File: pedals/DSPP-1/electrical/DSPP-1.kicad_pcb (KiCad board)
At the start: 2 copper layers, 4 parts, among them U1 STM32H747IGTx, U3 PCM3060, U4 STM32G4A1CETx, U5 STM32F401CBUx

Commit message: schematic update for MCU, Codec
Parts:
- removed U5: STM32F401CBUx, Package_DFN_QFN:QFN-48-1EP_7x7mm_P0.5mm_EP5.6x5.6mm
- added C10: 100n, Capacitor_SMD:C_0805_2012Metric, F.Cu at (148.9, 105.3)
- added C11: 10u, Capacitor_SMD:C_0805_2012Metric, F.Cu at (148.9, 108.3)
- added C12: 10u, Capacitor_SMD:C_0805_2012Metric, F.Cu at (148.9, 111.3)
- added C13: 100n, Capacitor_SMD:C_0805_2012Metric, F.Cu at (148.9, 114.3)
- added C14: 100n, Capacitor_SMD:C_0805_2012Metric, F.Cu at (153.3, 102.3)
- added C15: 10u, Capacitor_SMD:C_0805_2012Metric, F.Cu at (153.3, 105.3)
- added C16: 10u, Capacitor_SMD:C_0805_2012Metric, F.Cu at (153.3, 108.3)
- added C2: 100n, Capacitor_SMD:C_0805_2012Metric, F.Cu at (144.4, 102.3)
- added C3: 10u, Capacitor_SMD:C_0805_2012Metric, F.Cu at (144.4, 105.3)
- added C4: 10u, Capacitor_SMD:C_0805_2012Metric, F.Cu at (144.4, 108.3)
- added C5: 100p, Capacitor_SMD:C_0805_2012Metric, F.Cu at (144.4, 111.3)
- added C6: 100n, Capacitor_SMD:C_0805_2012Metric, F.Cu at (144.4, 114.3)
- added C7: 2.2n, Capacitor_SMD:C_0805_2012Metric, F.Cu at (148.9, 102.3)
- added J1: Guitar Jack, Connector_Audio:Jack_6.35mm_Neutrik_NMJ6HCD2_Horizontal, F.Cu at (150.1, 82.0)
- added JP1: Jumper, Jumper:SolderJumper-3_P1.3mm_Open_RoundedPad1.0x1.5mm, F.Cu at (158.4, 102.6)
- added JP2: Jumper, Jumper:SolderJumper-3_P1.3mm_Open_RoundedPad1.0x1.5mm, F.Cu at (158.4, 106.4)
- added JP3: Jumper, Jumper:SolderJumper-3_P1.3mm_Open_RoundedPad1.0x1.5mm, F.Cu at (158.4, 110.2)
- added R10: 100R, Resistor_SMD:R_0805_2012Metric, F.Cu at (177.4, 83.9)
- added R11: 0/220k, Resistor_SMD:R_0805_2012Metric, F.Cu at (177.4, 86.9)
- added R12: 10k, Resistor_SMD:R_0805_2012Metric, F.Cu at (177.4, 89.8)
- added R13: 10k, Resistor_SMD:R_0805_2012Metric, F.Cu at (177.4, 92.8)
- added R3: 100k, Resistor_SMD:R_0805_2012Metric, F.Cu at (173.0, 81.0)
- added R4: 100k, Resistor_SMD:R_0805_2012Metric, F.Cu at (173.0, 83.9)
- added R5: 1M, Resistor_SMD:R_0805_2012Metric, F.Cu at (173.0, 86.9)
- added R6: 1k, Resistor_SMD:R_0805_2012Metric, F.Cu at (173.0, 89.8)
- added R7: 2.2M, Resistor_SMD:R_0805_2012Metric, F.Cu at (173.0, 92.8)
- added R8: 100R, Resistor_SMD:R_0805_2012Metric, F.Cu at (173.0, 95.7)
- added R9: 100k, Resistor_SMD:R_0805_2012Metric, F.Cu at (177.4, 81.0)
- U1: value STM32H747IGTx -> STM32G474CBTx; footprint Package_QFP:LQFP-176_24x24mm_P0.5mm -> Package_QFP:LQFP-48_7x7mm_P0.5mm
- U4: value STM32G4A1CETx -> OPA1678; footprint Package_QFP:LQFP-48_7x7mm_P0.5mm -> Package_SON:SON-8-1EP_3x2mm_P0.5mm_EP1.4x1.6mm
- moved U4 67.6 mm to (174.9, 114.1)
- moved U3 49.2 mm to (176.9, 106.5)
- moved U1 48.9 mm to (166.9, 106.5)
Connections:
- U1 pad 12: Net-(U1-VSS-Pad100) -> unconnected-(U1-PA4-Pad12)
- U1 pad 23: unconnected-(U1-PF5-Pad23) -> Net-(U1-VSS-Pad23)
- U1 pad 24: Net-(U1-VSS-Pad100) -> unconnected-(U1-VDD-Pad24)
- U1 pad 35: unconnected-(U1-PC1-Pad35) -> Net-(U1-VSS-Pad23)
- U1 pad 45: Net-(U1-VSS-Pad100) -> unconnected-(U1-PB8-Pad45)
- U1 pad 47: Net-(U1-VSS-Pad100) -> Net-(U1-VSS-Pad23)
- U1 pad 6: Net-(U1-VSS-Pad100) -> unconnected-(U1-PF1-Pad6)
- U3 pad 1: unconnected-(U3-MC/SCL/FMT-Pad1) -> /SCL
- U3 pad 10: unconnected-(U3-BCK2-Pad10) -> /BCK
- U3 pad 11: unconnected-(U3-LRCK2-Pad11) -> /LRCK
- U3 pad 15: unconnected-(U3-~{RST}-Pad15) -> /~{RST}
- U3 pad 16: unconnected-(U3-SGND-Pad16) -> GND
- U3 pad 2: unconnected-(U3-MD/SDA/DEMP-Pad2) -> /SDA
- U3 pad 21: unconnected-(U3-V_{COM}-Pad21) -> Net-(U3-V_{COM})
- U3 pad 22: unconnected-(U3-AGND2-Pad22) -> GND
- U3 pad 23: unconnected-(U3-AGND1-Pad23) -> GND
- U3 pad 24: unconnected-(U3-V_{CC}-Pad24) -> +5VA
- U3 pad 25: unconnected-(U3-V_{IN}L-Pad25) -> /AUDIO_CODEC_IN
- U3 pad 26: unconnected-(U3-V_{IN}R-Pad26) -> Net-(U3-V_{IN}R)
- U3 pad 27: unconnected-(U3-~{MS}/AD/IFMD-Pad27) -> /ADRR
- U3 pad 28: unconnected-(U3-MODE-Pad28) -> Net-(U3-MODE)
- U3 pad 4: unconnected-(U3-LRCK1-Pad4) -> /LRCK
- U3 pad 5: unconnected-(U3-BCK1-Pad5) -> /BCK
- U3 pad 6: unconnected-(U3-SCKI1-Pad6) -> /SCKI
- U3 pad 7: unconnected-(U3-V_{DD}-Pad7) -> +3V3
- U3 pad 8: unconnected-(U3-DGND-Pad8) -> GND
- U3 pad 9: unconnected-(U3-SCKI2-Pad9) -> /SCKI
- U4 pad 1: unconnected-(U4-VBAT-Pad1) -> /AUDIO_BIAS
- U4 pad 2: unconnected-(U4-PC13-Pad2) -> /AUDIO_BIAS
- U4 pad 3: unconnected-(U4-PC14-Pad3) -> Net-(U4A-+)
- U4 pad 4: unconnected-(U4-PC15-Pad4) -> GND
- U4 pad 5: unconnected-(U4-PF0-Pad5) -> Net-(U4B-+)
- U4 pad 6: unconnected-(U4-PF1-Pad6) -> Net-(U4B--)
- U4 pad 7: unconnected-(U4-PG10-Pad7) -> Net-(U4B--)
- U4 pad 8: unconnected-(U4-PA0-Pad8) -> +5VA
- U4 pad 9: unconnected-(U4-PA1-Pad9) -> (no net)
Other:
- board outline added: 70.5 x 46 mm

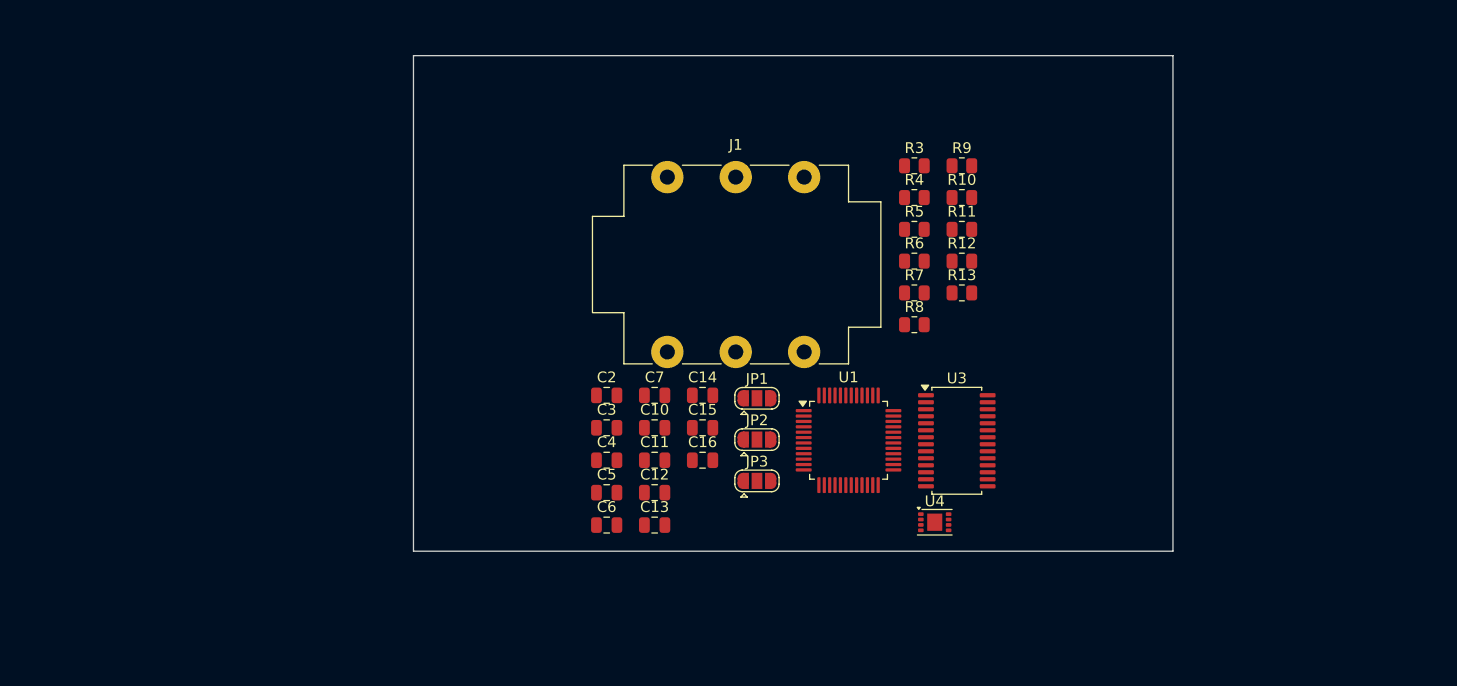
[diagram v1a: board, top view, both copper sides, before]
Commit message: Updated schematic, STM32 pinout
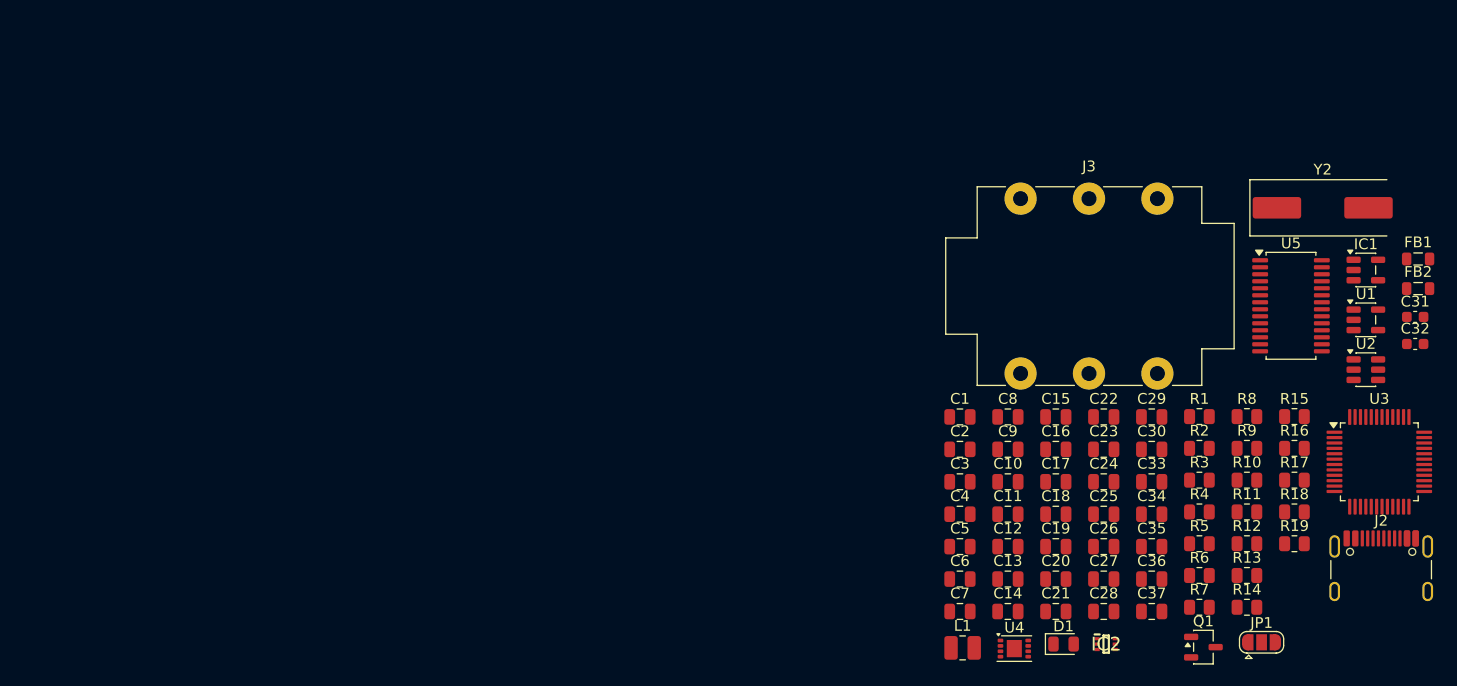
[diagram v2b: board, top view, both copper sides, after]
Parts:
- removed J1: Guitar Jack, Connector_Audio:Jack_6.35mm_Neutrik_NMJ6HCD2_Horizontal
- removed JP2, JP3: Jumper, Jumper:SolderJumper-3_P1.3mm_Open_RoundedPad1.0x1.5mm
- added C1: 10u, Capacitor_SMD:C_0805_2012Metric, F.Cu at (177.2, 104.3)
- added C17: 10u, Capacitor_SMD:C_0805_2012Metric, F.Cu at (186.1, 110.3)
- added C18: 100n, Capacitor_SMD:C_0805_2012Metric, F.Cu at (186.1, 113.3)
- added C19: 100p, Capacitor_SMD:C_0805_2012Metric, F.Cu at (186.1, 116.3)
- added C20: 100n, Capacitor_SMD:C_0805_2012Metric, F.Cu at (186.1, 119.3)
- added C21: 100n, Capacitor_SMD:C_0805_2012Metric, F.Cu at (186.1, 122.3)
- added C22: 10u, Capacitor_SMD:C_0805_2012Metric, F.Cu at (190.6, 104.3)
- added C23: 10u, Capacitor_SMD:C_0805_2012Metric, F.Cu at (190.6, 107.3)
- added C24: 10u, Capacitor_SMD:C_0805_2012Metric, F.Cu at (190.6, 110.3)
- added C25: 10u, Capacitor_SMD:C_0805_2012Metric, F.Cu at (190.6, 113.3)
- added C26: 100n, Capacitor_SMD:C_0805_2012Metric, F.Cu at (190.6, 116.3)
- added C27: 100n, Capacitor_SMD:C_0805_2012Metric, F.Cu at (190.6, 119.3)
- added C28: 10u, Capacitor_SMD:C_0805_2012Metric, F.Cu at (190.6, 122.3)
- added C29: 100n, Capacitor_SMD:C_0805_2012Metric, F.Cu at (195.0, 104.3)
- added C30: 10u, Capacitor_SMD:C_0805_2012Metric, F.Cu at (195.0, 107.3)
- added C31: 30p, Capacitor_SMD:C_0603_1608Metric, F.Cu at (219.5, 95.0)
- added C32: 30p, Capacitor_SMD:C_0603_1608Metric, F.Cu at (219.5, 97.5)
- added C33: 10u, Capacitor_SMD:C_0805_2012Metric, F.Cu at (195.0, 110.3)
- added C34: 100n, Capacitor_SMD:C_0805_2012Metric, F.Cu at (195.0, 113.3)
- added C35: 100n, Capacitor_SMD:C_0805_2012Metric, F.Cu at (195.0, 116.3)
- added C36: 100n, Capacitor_SMD:C_0805_2012Metric, F.Cu at (195.0, 119.3)
- added C37: 100n, Capacitor_SMD:C_0805_2012Metric, F.Cu at (195.0, 122.3)
- added C8: 22u, Capacitor_SMD:C_0805_2012Metric, F.Cu at (181.7, 104.3)
- added C9: 22u, Capacitor_SMD:C_0805_2012Metric, F.Cu at (181.7, 107.3)
- added D1: SD0805S020S0R5, Diode_SMD:D_0805_2012Metric, F.Cu at (186.8, 125.4)
- added FB1: 742792042, Inductor_SMD:L_0805_2012Metric, F.Cu at (219.8, 89.6)
- added FB2: 742792042, Inductor_SMD:L_0805_2012Metric, F.Cu at (219.8, 92.4)
- added IC1: TLV77333PDBVR, Package_TO_SOT_SMD:SOT-23-5, F.Cu at (214.9, 90.7)
- added IC2: TPS565247DRLR, SamacSys_Parts:SOTFL50P160X60-6N, F.Cu at (190.8, 125.4)
- added J2: USB_C, sumec_brd:USB_C_Receptacle_GCT_USB4105-xx-A_16P_TopMnt_Horizontal, F.Cu at (216.3, 119.4)
- added J3: Guitar Jack, Connector_Audio:Jack_6.35mm_Neutrik_NMJ6HCD2_Horizontal, F.Cu at (182.9, 84.0)
- added L1: 2.2u, Inductor_SMD:L_1008_2520Metric, F.Cu at (177.5, 125.7)
- added Q1: SI2393DS, Package_TO_SOT_SMD:SOT-23-3, F.Cu at (199.8, 125.7)
- added R1: 10k, Resistor_SMD:R_0805_2012Metric, F.Cu at (199.5, 104.3)
- added R14: 1k, Resistor_SMD:R_0805_2012Metric, F.Cu at (203.9, 122.0)
- added R15: 100k, Resistor_SMD:R_0805_2012Metric, F.Cu at (208.3, 104.3)
- added R16: 100k, Resistor_SMD:R_0805_2012Metric, F.Cu at (208.3, 107.2)
- added R17: 100k, Resistor_SMD:R_0805_2012Metric, F.Cu at (208.3, 110.2)
- added R18: 0/220k, Resistor_SMD:R_0805_2012Metric, F.Cu at (208.3, 113.1)
- added R19: 100R, Resistor_SMD:R_0805_2012Metric, F.Cu at (208.3, 116.1)
- added R2: 76.8k, Resistor_SMD:R_0805_2012Metric, F.Cu at (199.5, 107.2)
- added U2: USBLC6-2SC6, Package_TO_SOT_SMD:SOT-23-6, F.Cu at (214.9, 99.9)
- added U5: PCM3060, Package_SO:TSSOP-28_4.4x9.7mm_P0.65mm, F.Cu at (208.0, 94.0)
- added Y2: ABLS-12.288, Crystal:Crystal_SMD_HC49-SD, F.Cu at (210.9, 84.9)
- C11, C16, C3: value 10u -> 100n
- C13, C14: value 100n -> 22u
- C15: value 10u -> 22u
- C5: value 100p -> 10u
- C7: value 2.2n -> 100n
- R10: value 100R -> 10k
- R11: value 0/220k -> 10k
- R12: value 10k -> 2.2M
- R13: value 10k -> 1M
- R3: value 100k -> 10k
- R5: value 1M -> 100k
- R6: value 1k -> 5.1k
- R7: value 2.2M -> 15R
- R8: value 100R -> 15R
- R9: value 100k -> 5.1k
- U1: value STM32G474CBTx -> TPS7A2055PDBVRG4; footprint Package_QFP:LQFP-48_7x7mm_P0.5mm -> Package_TO_SOT_SMD:SOT-23-5
- U3: value PCM3060 -> STM32G474CBT6TR; footprint Package_SO:TSSOP-28_4.4x9.7mm_P0.65mm -> Package_QFP:LQFP-48_7x7mm_P0.5mm
- moved JP1 52.0 mm to (205.2, 125.2)
- moved U1 49.3 mm to (214.9, 95.3)
- moved R3 39.4 mm to (199.5, 110.2)
- moved R4 39.4 mm to (199.5, 113.1)
- moved R5 39.4 mm to (199.5, 116.1)
- moved R6 39.4 mm to (199.5, 119.0)
- moved R7 39.4 mm to (199.5, 122.0)
- moved U3 39.3 mm to (216.2, 108.5)
- moved R10 37.3 mm to (203.9, 110.2)
- moved R11 37.3 mm to (203.9, 113.1)
- moved R12 37.3 mm to (203.9, 116.1)
- moved R9 37.3 mm to (203.9, 107.2)
- moved R13 37.3 mm to (203.9, 119.0)
- moved C14 34.7 mm to (181.7, 122.3)
- moved C7 34.7 mm to (177.2, 122.3)
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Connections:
- C11 pad 1: GND -> +5V2
- C11 pad 2: +3V3 -> GND
- C12 pad 2: +5VA -> +3V3
- C13 pad 1: GND -> +5V2
- C13 pad 2: +5VA -> GND
- C14 pad 1: GND -> +5V2
- C14 pad 2: Net-(U3-V_{COM}) -> GND
- C15 pad 1: GND -> +5V2
- C15 pad 2: Net-(U3-V_{COM}) -> GND
- C16 pad 1: GND -> USB_VBUS
- C16 pad 2: Net-(U3-V_{IN}R) -> GND
- C2 pad 1: Net-(C2-Pad1) -> GND
- C2 pad 2: Net-(C2-Pad2) -> Net-(U1-EN)
- C3 pad 1: Net-(U4B--) -> GND
- C3 pad 2: Net-(C3-Pad2) -> +5VA
- C4 pad 1: Net-(U4A-+) -> GND
- C4 pad 2: GND -> +5VA
- C5 pad 2: Net-(C2-Pad1) -> +5V2
- C6 pad 2: +5VA -> +5V2
- C7 pad 1: Net-(C7-Pad1) -> VCC
- R10 pad 1: Net-(C3-Pad2) -> +3V3
- R10 pad 2: /AUDIO_CODEC_IN -> /SDA
- R11 pad 1: Net-(JP1-C) -> +3V3
- R11 pad 2: Net-(U3-MODE) -> /SCL
- R12 pad 1: +3V3 -> GND
- R12 pad 2: /SDA -> Net-(C19-Pad2)
- R13 pad 1: +3V3 -> /AUDIO_BIAS
- R13 pad 2: /SCL -> Net-(C21-Pad2)
- R3 pad 1: +5VA -> GND
- R3 pad 2: Net-(U4A-+) -> Net-(IC2-FB)
- R4 pad 1: Net-(U4A-+) -> Net-(IC2-EN)
- R4 pad 2: GND -> VCC
- R5 pad 1: /AUDIO_BIAS -> GND
- R5 pad 2: Net-(C2-Pad2) -> Net-(IC2-EN)
- R6 pad 1: Net-(C2-Pad2) -> GND
- R6 pad 2: Net-(U4B-+) -> Net-(J2-CC2)
- R7 pad 1: GND -> Net-(J2-D--PadA7)
- R7 pad 2: Net-(C2-Pad1) -> /DN_IN
- R8 pad 1: /AUDIO_CODEC_IN -> Net-(J2-D+-PadA6)
- R8 pad 2: Net-(C7-Pad1) -> /DP_IN
- R9 pad 2: Net-(C3-Pad2) -> Net-(J2-CC1)
- U1 pad 1: unconnected-(U1-VBAT-Pad1) -> Net-(U1-EN)
- U1 pad 2: unconnected-(U1-PC13-Pad2) -> GND
- U1 pad 3: unconnected-(U1-PC14-Pad3) -> Net-(U1-EN)
- U1 pad 5: unconnected-(U1-PF0-Pad5) -> +5VA
- U3 pad 1: /SCL -> +3V3
- U3 pad 10: /BCK -> unconnected-(U3-PA2-Pad10)
- U3 pad 11: /LRCK -> /SAI_MCLK_A
- U3 pad 15: /~{RST} -> unconnected-(U3-PA7-Pad15)
- U3 pad 16: GND -> unconnected-(U3-PB0-Pad16)
- U3 pad 2: /SDA -> unconnected-(U3-PC13-Pad2)
- U3 pad 20: unconnected-(U3-V_{OUT}L+-Pad20) -> /VDDA
- U3 pad 21: Net-(U3-V_{COM}) -> /VDDA
- U3 pad 22: GND -> /SAI_SCK_A
- U3 pad 24: +5VA -> +3V3
- U3 pad 25: /AUDIO_CODEC_IN -> unconnected-(U3-PB11-Pad25)
- U3 pad 26: Net-(U3-V_{IN}R) -> unconnected-(U3-PB12-Pad26)
- U3 pad 27: /ADRR -> unconnected-(U3-PB13-Pad27)
- U3 pad 28: Net-(U3-MODE) -> unconnected-(U3-PB14-Pad28)
- U3 pad 4: /LRCK -> unconnected-(U3-PC15-Pad4)
- U3 pad 5: /BCK -> Net-(U3-PF0)
- U3 pad 6: /SCKI -> Net-(U3-PF1)
- U3 pad 7: +3V3 -> /NRST
- U3 pad 8: GND -> unconnected-(U3-PA0-Pad8)
- U3 pad 9: /SCKI -> unconnected-(U3-PA1-Pad9)
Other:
- board outline removed
